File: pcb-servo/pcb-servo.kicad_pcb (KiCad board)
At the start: 2 copper layers, 61 x 62 mm, 25 parts, among them J1 PWM, J10 PWM, J11 PWM, J12 PWM, J13 PWM, J14 PWM, J15 PWM, J16 PWM, J17 LEFT-EXT, J18 RIGHT-EXT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

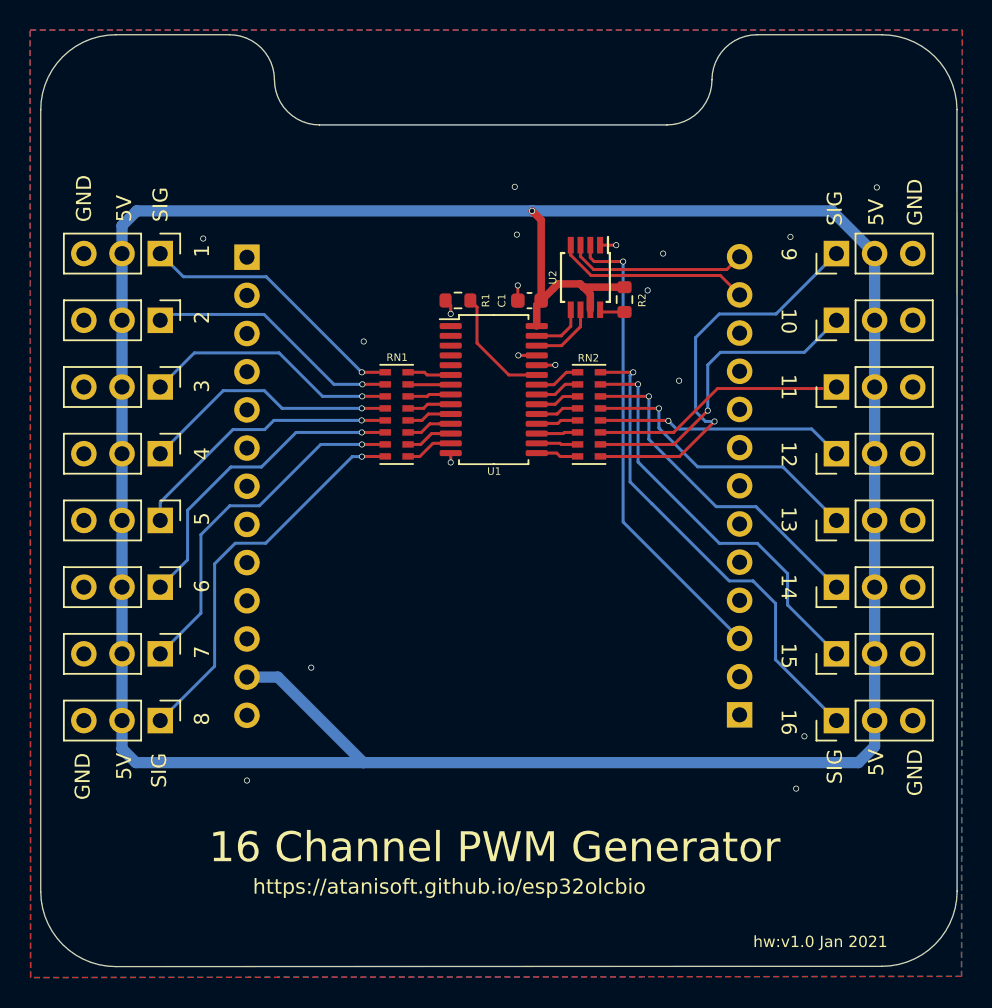
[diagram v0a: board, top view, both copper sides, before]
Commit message: :pencil: adjust PCB to use a cut out instead of solid panel
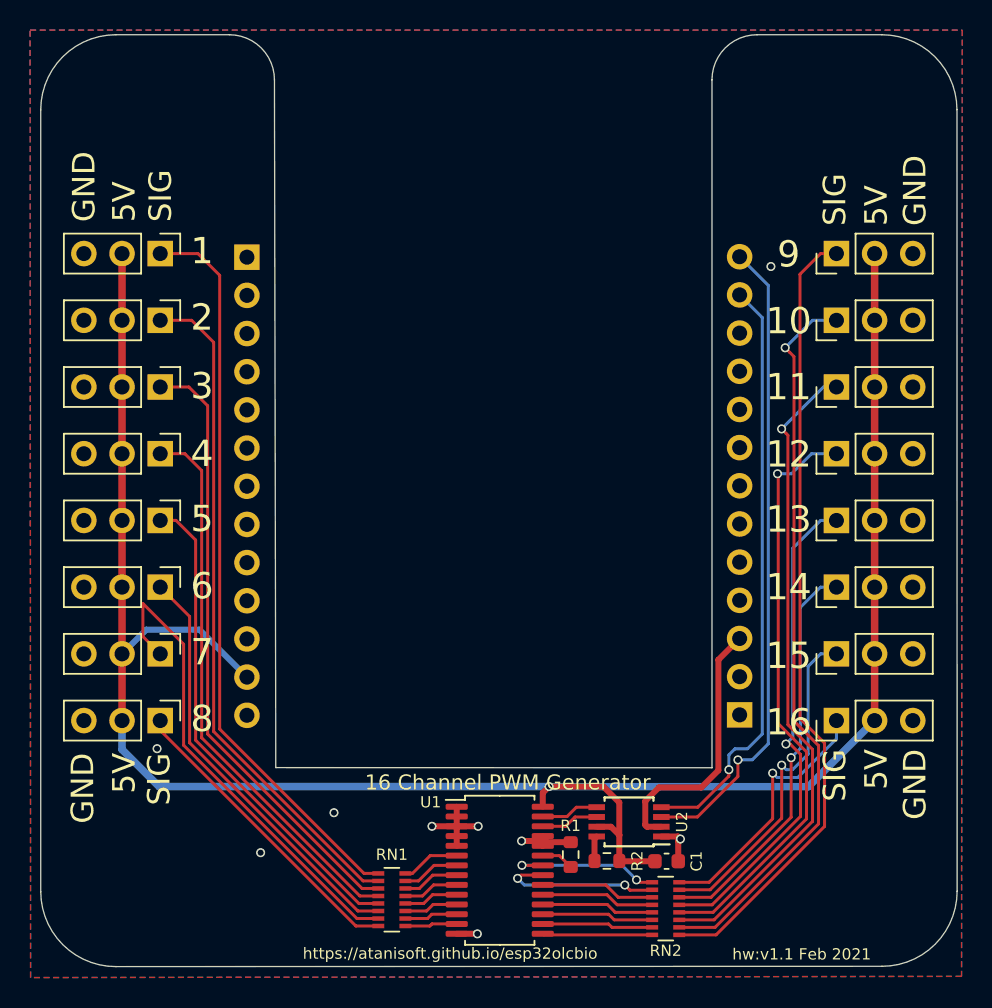
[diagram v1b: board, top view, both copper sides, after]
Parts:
- RN1, RN2: footprint Resistor_SMD:R_Cat16-8 -> Resistor_SMD:R_Array_Convex_8x0602
- moved C1 38.4 mm to (148.3, 103.2), turned to 0 degrees
- moved R1 37.6 mm to (141.9, 102.8), turned to 90 degrees
- moved R2 37.4 mm to (144.3, 103.2), turned to 180 degrees
- moved U2 36.3 mm to (145.8, 100.6), turned to 180 degrees
- moved RN2 33.3 mm to (148.3, 106.4)
- moved RN1 32.3 mm to (130.0, 105.8)
- moved U1 32.0 mm to (137.2, 103.8)
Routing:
- net +5V: track 197.5 -> 141.9 mm
- net PWM-1: track 18.2 -> 49.3 mm, vias 1 -> 0
- net I2C_SCL: track 12.0 -> 43.0 mm, vias 0 -> 1
- net PWM-2: track 17.1 -> 45.1 mm, vias 1 -> 0
- net PWM-10: track 20.9 -> 48.9 mm
- net PWM-11: track 17.0 -> 43.4 mm, vias 0 -> 1
- net I2C_SDA: track 13.0 -> 39.4 mm, vias 0 -> 1
- net PWM-9: track 26.7 -> 53.1 mm, vias 1 -> 0
- net PWM-3: track 17.1 -> 41.1 mm, vias 1 -> 0
- net PWM-12: track 16.6 -> 39.3 mm
- net PWM-4: track 17.2 -> 37.1 mm, vias 1 -> 0
- net PWM-5: track 18.4 -> 32.9 mm, vias 1 -> 0
- net PWM-16: track 32.1 -> 17.7 mm
- net +3V3: track 31.4 -> 17.8 mm, vias 1 -> 0
- net PWM-13: track 19.6 -> 32.8 mm
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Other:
- outline, holes or cut-outs redrawn
- board text added: "hw:v1.1 Feb 2021"
- board text removed: "hw:v1.0 Jan 2021"

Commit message: :tractor: Update with current PCB in testing.
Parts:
- added C2: DNP, Capacitor_THT:CP_Radial_D8.0mm_P3.50mm, F.Cu at (113.3, 53.1)
- added C3: DNP, Capacitor_THT:CP_Radial_D8.0mm_P3.50mm, F.Cu at (164.0, 53.1)
- added C4: DNP, Capacitor_THT:CP_Radial_D8.0mm_P3.50mm, F.Cu at (164.0, 105.1)
- added C5: DNP, Capacitor_THT:CP_Radial_D8.0mm_P3.50mm, F.Cu at (113.3, 105.1)
- moved R2 2.24 mm to (146.6, 103.1)
- moved U2 2.24 mm to (148.1, 100.5)
- moved R1 1.42 mm to (143.3, 102.6), turned to 0 degrees
- moved C1 1.30 mm to (149.6, 103.1)
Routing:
- net +5V: track 141.9 -> 187.3 mm, vias 1 -> 2
- net GND: track 13.9 -> 51.8 mm, vias 9 -> 21
- net PWM-7: track 32.1 -> 25.5 mm
- net Net-(RN2-Pad2): track 11.1 -> 7.68 mm, vias 2 -> 0
- net Net-(RN2-Pad1): track 10.5 -> 7.74 mm, vias 2 -> 0
- net 5V_I2C_SCL: track 3.84 -> 6.14 mm
- net 5V_I2C_SDA: track 3.84 -> 6.14 mm
- net PWM-13: track 32.8 -> 31.2 mm
- net PWM-12: track 39.3 -> 37.8 mm
- net PWM-9: track 53.1 -> 51.7 mm
- net PWM-10: track 48.9 -> 47.6 mm
- net PWM-16: track 17.7 -> 18.8 mm
- net PWM-1: track 49.3 -> 50.4 mm
- net PWM-2: track 45.1 -> 46.2 mm
- net PWM-8: track 20.6 -> 21.6 mm
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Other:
- board text added: "hw:v1.1 July 2021"
- board text removed: "hw:v1.1 Feb 2021"

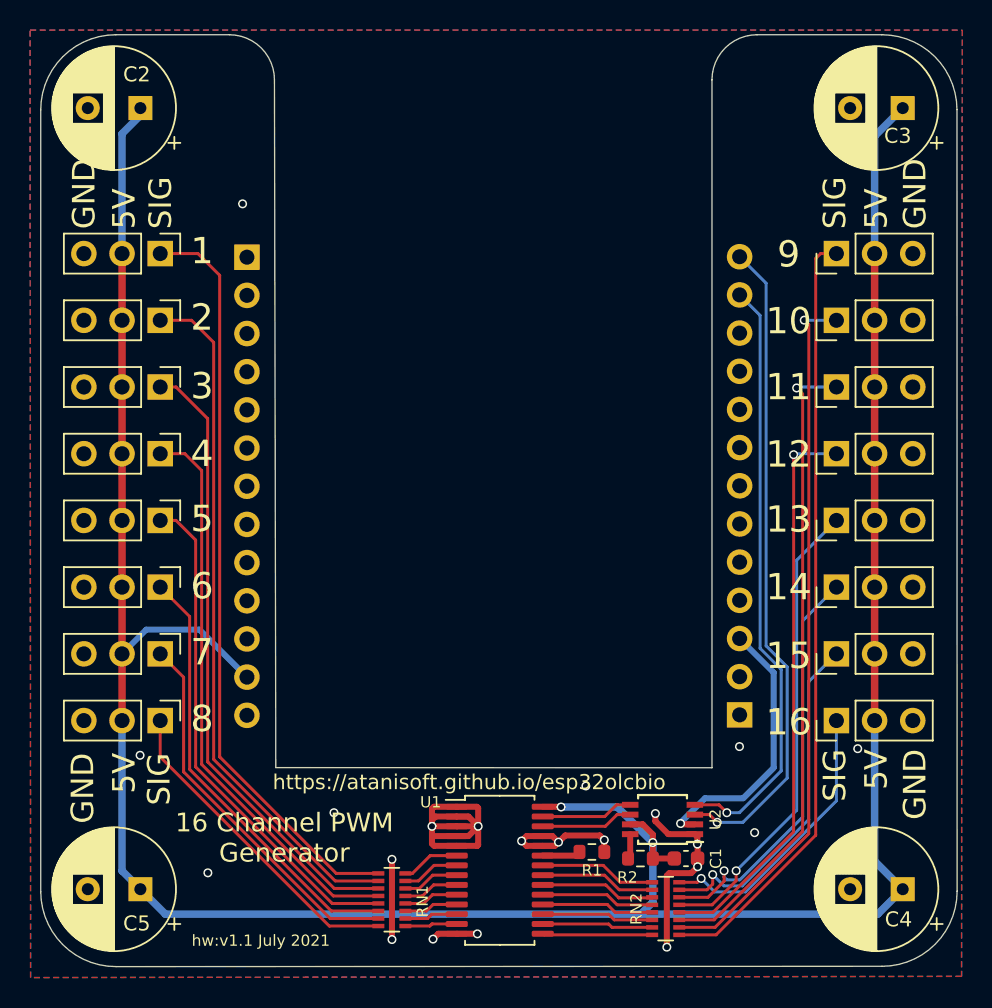
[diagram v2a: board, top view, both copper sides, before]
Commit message: PCB updates for KiCad6
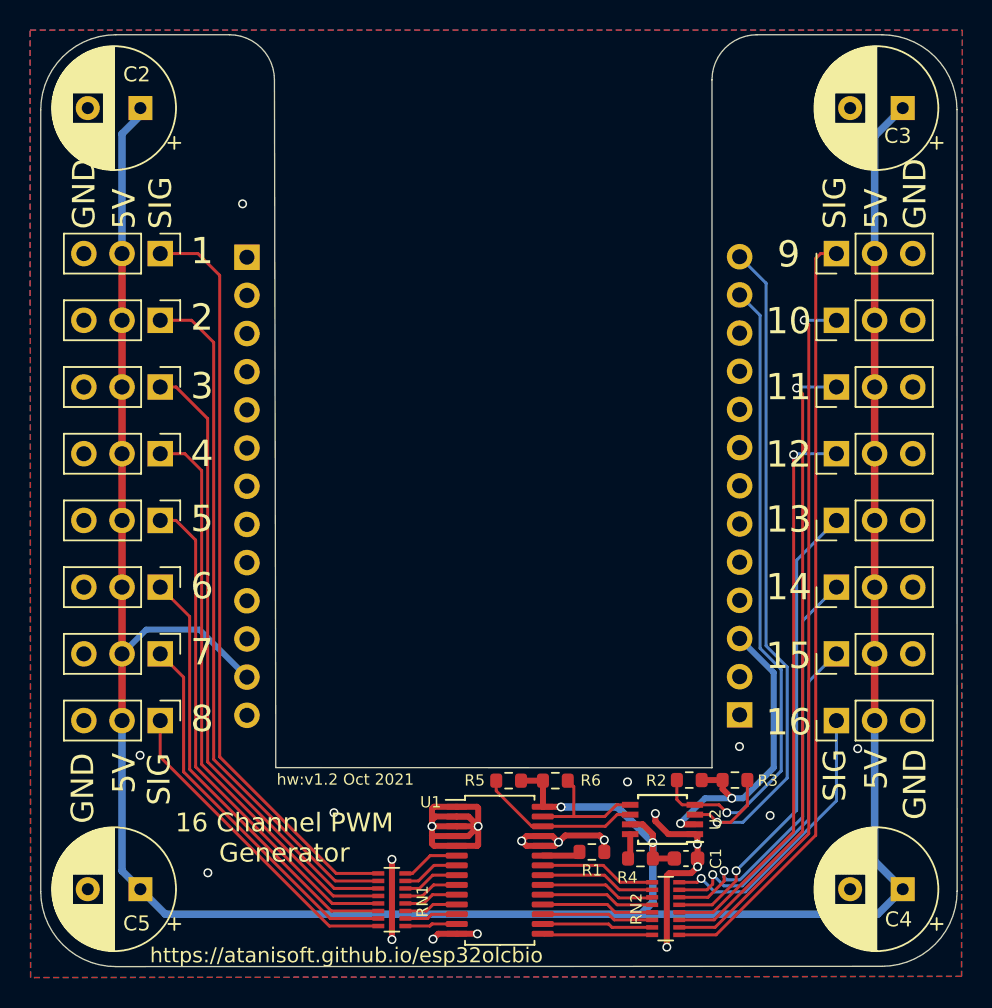
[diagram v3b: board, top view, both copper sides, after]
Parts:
- added R2: 2K4, Resistor_SMD:R_0603_1608Metric, F.Cu at (149.8, 97.8)
- added R3: 2K4, Resistor_SMD:R_0603_1608Metric, F.Cu at (152.9, 97.8)
- added R5: 4k7, Resistor_SMD:R_0603_1608Metric, F.Cu at (137.8, 97.9)
- added R6: 4k7, Resistor_SMD:R_0603_1608Metric, F.Cu at (140.9, 97.9)
- renumbered R2 to R4
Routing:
- net 5V_I2C_SCL: track 6.14 -> 10.9 mm
- net I2C_SCL: track 43.6 -> 47.7 mm
- net +5V: track 187.3 -> 190.5 mm
- net +3V3: track 18.3 -> 21.1 mm, vias 1 -> 2
- net I2C_SDA: track 39.9 -> 42.6 mm
- net 5V_I2C_SDA: track 6.14 -> 8.69 mm
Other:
- net class Default removed
- board text added: "hw:v1.2 Oct 2021"
